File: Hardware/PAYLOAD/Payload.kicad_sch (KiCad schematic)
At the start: 3 parts

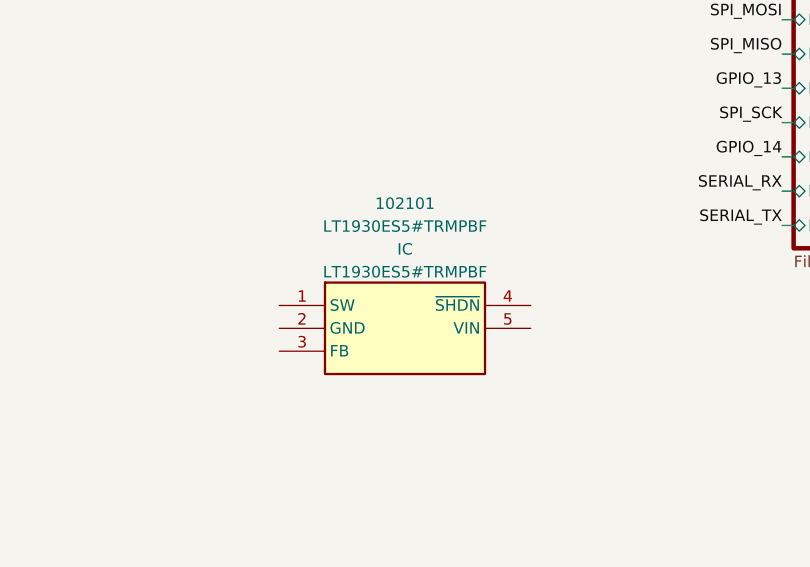
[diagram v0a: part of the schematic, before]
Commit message: Updated to KiCAD 7.0
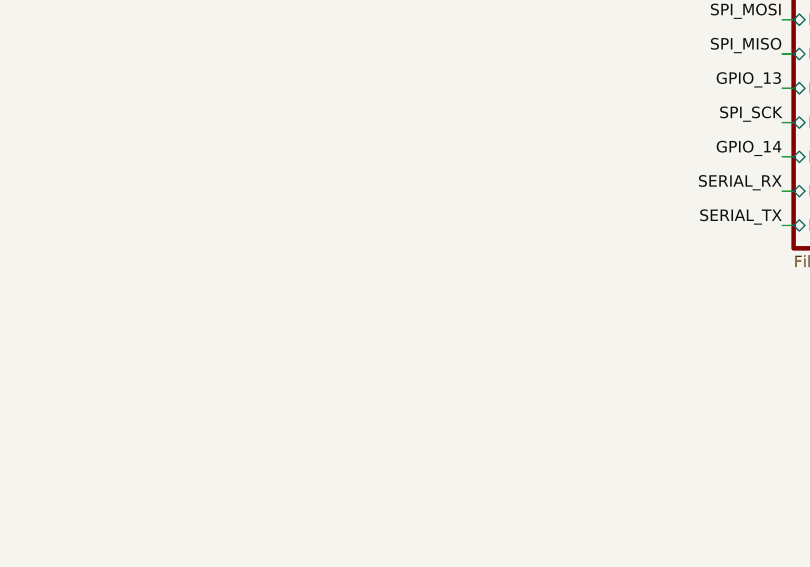
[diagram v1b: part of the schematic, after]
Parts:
- removed 102101: LT1930ES5#TRMPBF, LT1930ES5#TRMPBF:SOT95P280X145-5N, symbol LT1930ES5#TRMPBF:LT1930ES5#TRMPBF
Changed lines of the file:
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@@
     (pin "1")
-  )
-  (symbol (lib_id "LT1930ES5#TRMPBF:LT1930ES5#TRMPBF") (at 162.56 134.62 0) (unit 1)
-    (in_bom yes) (on_board yes) (fields_autoplaced)
-    (property "Reference" "102101" (id 0) (at 176.53 123.3064 0))
-    (property "Value" "LT1930ES5#TRMPBF" (id 1) (at 176.53 125.8433 0))
-    (property "Footprint" "LT1930ES5#TRMPBF:SOT95P280X145-5N" (id 2) (at 162.56 134.62 0)
-      (effects (font (size 1.27 1.27)) hide)
-    )
-    (property "Datasheet" "" (id 3) (at 162.56 134.62 0)
-      (effects (font (size 1.27 1.27)) hide)
-    )
-    (property "Reference_1" "IC" (id 4) (at 176.53 128.3802 0))
-    (property "Value_1" "LT1930ES5#TRMPBF" (id 5) (at 176.53 130.9171 0))
-    (property "Footprint_1" "SOT95P280X145-5N" (id 6) (at 186.69 229.54 0)
-      (effects (font (size 1.27 1.27)) (justify left top) hide)
-    )
-    (property "Datasheet_1" "https://datasheet.datasheetarchive.com/originals/distributors/SFDatasheet-4/sf-00091027.pdf" (id 7) (at 186.69 329.54 0)
-      (effects (font (size 1.27 1.27)) (justify left top) hide)
-    )
-    (property "Height" "1.45" (id 8) (at 186.69 529.54 0)
-      (effects (font (size 1.27 1.27)) (justify left top) hide)
-    )
-    (property "Manufacturer_Name" "Analog Devices" (id 9) (at 186.69 629.54 0)
-      (effects (font (size 1.27 1.27)) (justify left top) hide)
-    )
-    (property "Manufacturer_Part_Number" "LT1930ES5#TRMPBF" (id 10) (at 186.69 729.54 0)
-      (effects (font (size 1.27 1.27)) (justify left top) hide)
-    )
-    (property "Mouser Part Number" "584-LT1930ES5#TRMPBF" (id 11) (at 186.69 829.54 0)
-      (effects (font (size 1.27 1.27)) (justify left top) hide)
-    )
-    (property "Mouser Price/Stock" "https://www.mouser.co.uk/ProductDetail/Analog-Devices/LT1930ES5TRMPBF?qs=ytflclh7QUXsZW533VXHKw%3D%3D" (id 12) (at 186.69 929.54 0)
-      (effects (font (size 1.27 1.27)) (justify left top) hide)
-    )
-    (property "Arrow Part Number" "LT1930ES5#TRMPBF" (id 13) (at 186.69 1029.54 0)
-      (effects (font (size 1.27 1.27)) (justify left top) hide)
-    )
-    (property "Arrow Price/Stock" "https://www.arrow.com/en/products/lt1930es5trmpbf/analog-devices?region=nac" (id 14) (at 186.69 1129.54 0)
-      (effects (font (size 1.27 1.27)) (justify left top) hide)
-    )
-    (pin "1")
-    (pin "2")
-    (pin "3")
-    (pin "4")
-    (pin "5")
   )
   (sheet (at 219.71 88.9) (size 12.7 39.37) (fields_autoplaced)
@@
       (reference "101101") (unit 1) (value "RM-VT02") (footprint "RM-VT02:RMVT02")
     )
-    (path "/e86b9afb-c6d8-4ae8-9836-99c872fc462d"
-      (reference "102101") (unit 1) (value "LT1930ES5#TRMPBF") (footprint "LT1930ES5#TRMPBF:SOT95P280X145-5N")
-    )
     (path "/284eefa5-a591-4943-9a8e-a7847e2a597d/c5e47bd0-73f1-4697-b4e4-c6b853a0d810"
       (reference "C201") (unit 1) (value "4.7uF") (footprint "Capacitor_SMD:C_0603_1608Metric_Pad1.08x0.95mm_HandSolder")
@@
     )
     (path "/284eefa5-a591-4943-9a8e-a7847e2a597d/006050d5-72eb-4925-99bb-5af0b3e44475"
-      (reference "J201") (unit 1) (value "Conn_ARM_JTAG_SWD_10") (footprint "digikey-footprints:PinHeader_2x5_P1.27mm_Drill.7mm")
+      (reference "J201") (unit 1) (value "Conn_ARM_JTAG_SWD_10") (footprint "Connector_PinHeader_2.00mm:PinHeader_2x05_P2.00mm_Vertical")
     )
     (path "/5f789805-2281-4e3f-97bc-cfcf0a869a8a/d22e2b21-7d00-4660-babe-d9ca29678fb6"
@@
       (reference "R209") (unit 1) (value "3.3k") (footprint "Resistor_SMD:R_0603_1608Metric_Pad0.98x0.95mm_HandSolder")
     )
-    (path "/284eefa5-a591-4943-9a8e-a7847e2a597d/d79672f9-3c64-4944-a9f6-124c35699c8d"
-      (reference "R210") (unit 1) (value "22") (footprint "Resistor_SMD:R_0603_1608Metric_Pad0.98x0.95mm_HandSolder")
-    )
-    (path "/284eefa5-a591-4943-9a8e-a7847e2a597d/4e0797b0-6833-4fb7-b6fc-9cc38c613976"
-      (reference "R211") (unit 1) (value "22") (footprint "Resistor_SMD:R_0603_1608Metric_Pad0.98x0.95mm_HandSolder")
-    )
-    (path "/284eefa5-a591-4943-9a8e-a7847e2a597d/2e873d54-da44-405c-94a9-f25112d32c23"
-      (reference "R212") (unit 1) (value "22") (footprint "Resistor_SMD:R_0603_1608Metric_Pad0.98x0.95mm_HandSolder")
-    )
-    (path "/284eefa5-a591-4943-9a8e-a7847e2a597d/c146b6d4-54c6-4d3e-8a6f-b480d8735d5a"
-      (reference "R213") (unit 1) (value "22") (footprint "Resistor_SMD:R_0603_1608Metric_Pad0.98x0.95mm_HandSolder")
-    )
-    (path "/284eefa5-a591-4943-9a8e-a7847e2a597d/8126e208-9fe9-4421-8046-f277121a02db"
-      (reference "R214") (unit 1) (value "22") (footprint "Resistor_SMD:R_0603_1608Metric_Pad0.98x0.95mm_HandSolder")
-    )
     (path "/5f789805-2281-4e3f-97bc-cfcf0a869a8a/0a763314-daf4-4df2-b5f4-013f43e7793f"
       (reference "R401") (unit 1) (value "5.1k") (footprint "Resistor_SMD:R_0603_1608Metric_Pad0.98x0.95mm_HandSolder")
@@
       (reference "U401") (unit 1) (value "AP7361C-33Y5-13") (footprint "AP7361C-25Y5-13:AP7361C25Y513")
     )
+    (path "/a4effa76-f80b-4d3f-a900-97530ceb36a5/3d3276a2-dc5a-4d6a-bf65-5f92c669efe2"
+      (reference "U?") (unit 1) (value "LT1930ES5#TRMPBF") (footprint "LT1930ES5#TRMPBF:SOT95P280X145-5N")
+    )
     (path "/284eefa5-a591-4943-9a8e-a7847e2a597d/dbc0456c-021d-47c8-9714-55619d0e7ccf"
